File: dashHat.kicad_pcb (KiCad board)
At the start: 4 copper layers, 65 x 56 mm, 142 parts, among them J1 Input, J2 LCD, J3 GPIO, J4 LEDs, J5 Ride Through, J6 SMA, J7 Conn_01x08, Q1 BSS138, Q2 BSS138, Q3 2N7002, Q4 BSS84, Q5 BSS84, Q6 BSS84, Q7 , Q8 , U1 CAT24C256, U10 CPC1017N, U11 CPC1017N, U12 MAX22193, U13 IX4427, U2 MAX17614, U3 TVS3300DRV, U4 LM61480, U5 74LVC1G80, U6 ZOE-M8Q, U7 TCAN330, U8 MCP2515-xST, U9 MAX3227, Y1 32.768k, Y2 8MHz

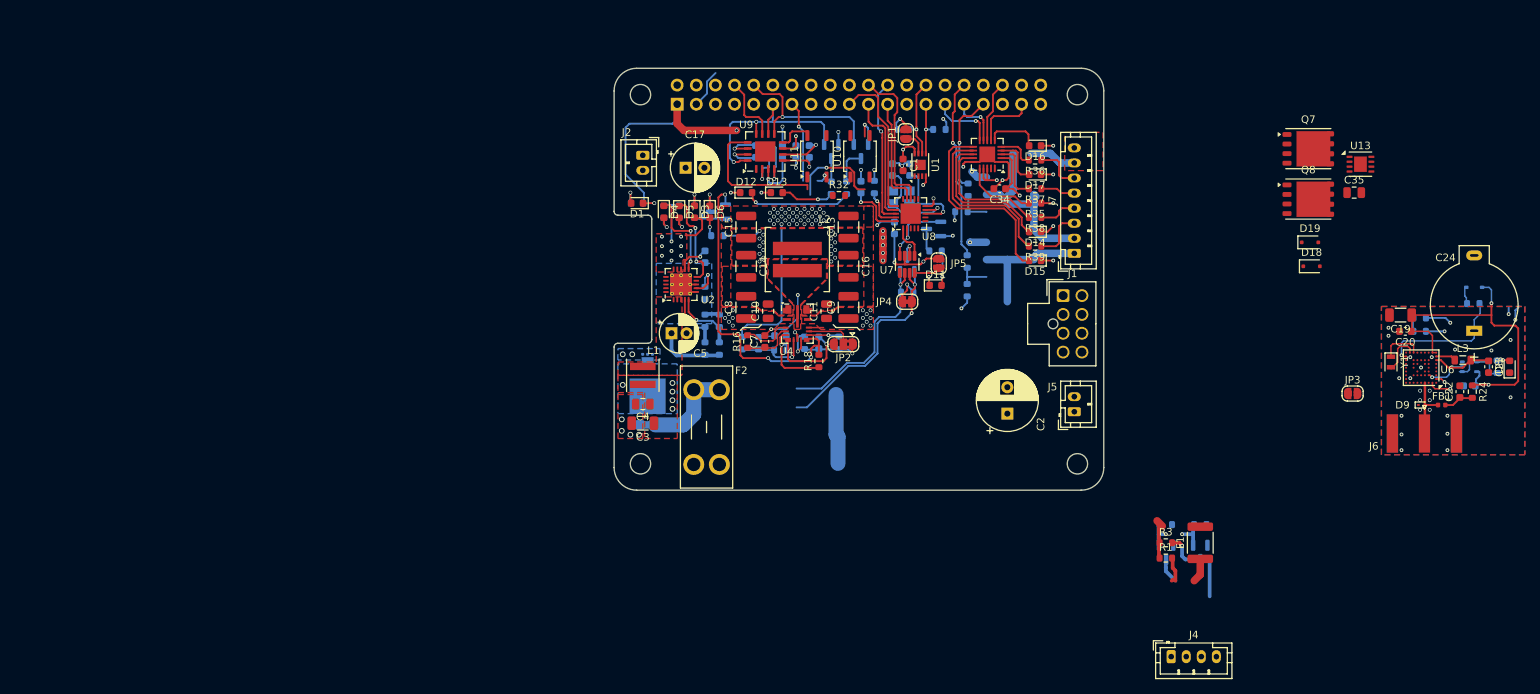
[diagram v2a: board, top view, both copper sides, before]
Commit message: second pass at layout complete
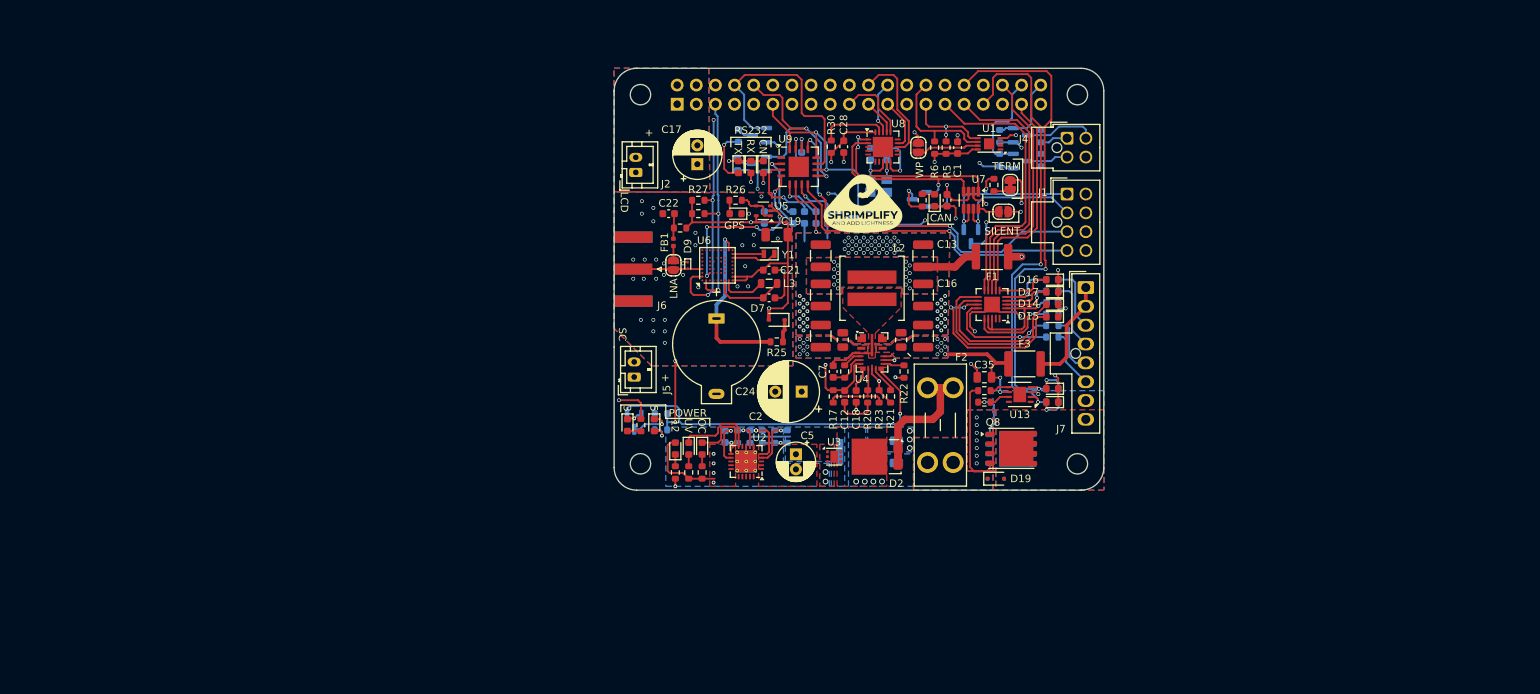
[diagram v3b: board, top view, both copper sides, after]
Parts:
- removed JP2: FPWM, Jumper:SolderJumper-3_P1.3mm_Bridged2Bar12_RoundedPad1.0x1.5mm
- removed R41, R43: 10k, Resistor_SMD:R_0603_1608Metric
- removed U10, U11: CPC1017N, Package_SO:SOP-4_3.8x4.1mm_P2.54mm
- added D20: Green, LED_SMD:LED_0603_1608Metric, F.Cu at (158.2, 86.5)
- added D21: Green, LED_SMD:LED_0603_1608Metric, F.Cu at (158.2, 88.3)
- added D22: Green, LED_SMD:LED_0603_1608Metric, F.Cu at (116.5, 57.1)
- added F3: 0.2A, Fuse:Fuse_1812_4532Metric, F.Cu at (154.5, 83.2)
- added Q9: BSS84, Package_TO_SOT_SMD:SOT-23, B.Cu at (119.3, 52.9)
- added R44: 1k, Resistor_SMD:R_0603_1608Metric, B.Cu at (158.2, 88.3)
- added R45: 1k, Resistor_SMD:R_0603_1608Metric, B.Cu at (158.2, 86.5)
- C12, C18, C21, C25, C28, D2, D7, R10, R11, R12, R17, R20, R21, R22, R23, R25, R26, R27, R28, R29, R30, R31, R40, R42, R5, R6, R7, U3, U5: moved to F.Cu
- C20, C3, C34, C4, D18, L1, Q7, R1, R18, R3, R35, R36, R37, R38, R39: moved to B.Cu
- J4: footprint Connector_JST:JST_PH_B4B-PH-K_1x04_P2.00mm_Vertical -> Connector_Molex:Molex_Nano-Fit_105310-xx04_2x02_P2.50mm_Vertical
- J7: footprint Connector_JST:JST_PH_B8B-PH-K_1x08_P2.00mm_Vertical -> Connector_Molex:Molex_Nano-Fit_105309-xx08_1x08_P2.50mm_Vertical
- R32: value 1k -> 220; moved to B.Cu
- moved C22 107.7 mm to (107.2, 63.3), turned to 180 degrees
- moved R24 107.4 mm to (108.8, 65.2), turned to 0 degrees
- moved J6 107.3 mm to (102.5, 70.7), turned to 180 degrees
- moved D8 104.7 mm to (116.1, 63.3), turned to 180 degrees
- moved FB1 104.2 mm to (107.9, 67.1), turned to 90 degrees
- moved R26 103.5 mm to (116.1, 61.5), turned to 180 degrees
- moved C24 100.6 mm to (113.6, 77.2), turned to -90 degrees
- moved D9 99.2 mm to (109.8, 70.2), turned to -90 degrees
- moved R27 97.0 mm to (111.2, 61.5)
- moved R28 97.0 mm to (111.2, 63.3)
- moved U5 96.0 mm to (119.8, 62.9), turned to 180 degrees
- moved C23 95.9 mm to (120.6, 74.5), turned to 0 degrees
- moved U6 94.4 mm to (113.7, 70.2), turned to 90 degrees
- moved C21 94.2 mm to (120.6, 70.8), turned to 0 degrees
- moved D7 92.7 mm to (121.6, 77.4), turned to 180 degrees
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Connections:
- D10 pad 1: /CAN/CANH -> /CAN/CANL
- D10 pad 2: /CAN/CANL -> /CAN/CANH
- D18 pad 1: /GPIO/+12V_{raw} -> +12P
- D19 pad 1: /GPIO/+12V_{raw} -> +12P
- F2 pad 1: /Power/+12V_{raw} -> +12P
- J1 pad 1: /RS232/232TX -> /CAN/CANL
- J1 pad 2: /RS232/232RX -> /CAN/CANH
- J1 pad 3: /CAN/CANH -> /RS232/232TX
- J1 pad 4: /CAN/CANL -> /RS232/232RX
- J1 pad 5: /GPIO/+12V_{raw} -> GND
- J1 pad 6: /GPIO/+12V_{raw} -> GND
- J1 pad 7: GND -> +12P
- J1 pad 8: GND -> +12P
- J7 pad 1: Net-(D19-A) -> Net-(J7-Pin_1)
- J7 pad 2: Net-(D18-A) -> Net-(J7-Pin_1)
- J7 pad 7: +12V -> Net-(D18-A)
- J7 pad 8: +12V -> Net-(D19-A)
- Q7 pad 1: Net-(Q7-G) -> GND
- Q7 pad 2: Net-(D18-A) -> Net-(Q7-G)
- Q7 pad 3: GND -> Net-(D18-A)
- Q8 pad 1: Net-(Q8-G) -> GND
- Q8 pad 2: Net-(D19-A) -> Net-(Q8-G)
- Q8 pad 3: GND -> Net-(D19-A)
- R1 pad 1: +5V -> Net-(J4-Pin_1)
- R3 pad 1: +5V -> Net-(J4-Pin_1)
- R32 pad 1: /GPIO27 -> Net-(Q9-D)
- R36 pad 1: Net-(J7-Pin_6) -> Net-(J7-Pin_3)
- R37 pad 1: Net-(J7-Pin_5) -> Net-(J7-Pin_4)
- R38 pad 1: Net-(J7-Pin_4) -> Net-(J7-Pin_5)
- R38 pad 2: Net-(U12-IN4) -> Net-(U12-IN3)
- R39 pad 1: Net-(J7-Pin_3) -> Net-(J7-Pin_6)
- R39 pad 2: Net-(U12-IN3) -> Net-(U12-IN4)
- U12 pad 11: Net-(D15-A) -> Net-(D14-A)
- U12 pad 13: Net-(D14-A) -> Net-(D15-A)
- U4 pad 12: Net-(JP2-C) -> GND
- U9 pad 13: Net-(U9-T1OUT) -> /RS232/232TX
- U9 pad 8: Net-(U9-R1IN) -> /RS232/232RX
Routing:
- net /RS232/232TX: track 0.00 -> 49.2 mm, vias 0 -> 3
- net /GPIO13/PWM1: track 13.3 -> 61.1 mm, vias 1 -> 2
- net /RS232/232RX: track 0.00 -> 41.8 mm, vias 0 -> 1
- net +12V: track 68.6 -> 28.0 mm, vias 23 -> 22
- net /GPIO12/PWM0: track 23.9 -> 62.9 mm, vias 1 -> 2
- net +3V3: track 144.3 -> 183.0 mm, vias 18 -> 15
- net (no net): track 30.2 -> 0.00 mm, vias 1 -> 0
- net /GPIO5: track 8.70 -> 37.3 mm, vias 1 -> 0
- net /GPIO6: track 7.04 -> 35.6 mm, vias 1 -> 0
- net /GPIO16: track 8.17 -> 33.2 mm
- net Net-(J4-Pin_1): track 3.14 -> 28.0 mm, vias 0 -> 1
- net Net-(D18-A): track 24.4 -> 0.00 mm
- net /GPIO14/TXD0: track 8.98 -> 33.0 mm
- net Net-(U7-TXD): track 4.71 -> 26.3 mm, vias 0 -> 2
- net /GPIO26: track 8.41 -> 29.9 mm
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- added copper zone on B.Cu, net +12P
- added copper zone on F.Cu, net +12P
- added copper zone on In2.Cu, net +12P
- added copper zone on B.Cu, net +12V
- added copper zone on In1.Cu, net +12V
- added copper zone on B.Cu, net +5V
- added copper zone on In1.Cu, net +5V
- added copper zone on In2.Cu, net GND
- added copper zone on B.Cu, net IN
- added copper zone on B.Cu, net Net-(D18-A)
- added copper zone on F.Cu, net Net-(D19-A)
- removed copper zone on F.Cu, net /GPIO/+12V_{raw}
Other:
- outline, holes or cut-outs redrawn
- board text added: "+"
- board text added: "12"
- board text added: "3"
- board text added: "5"
- board text added: "CAN"
- board text added: "CN"
- board text added: "GPS"
- board text added: "LCD"
- board text added: "LNA"
- board text added: "OC"
- board text added: "POWER"
- board text added: "RS232"
- board text added: "RX"
- board text added: "SC"
- board text added: "SILENT"
- board text added: "TERM"
- board text added: "TX"
- board text added: "UV"
- board text added: "WP"
- board text removed: "DISPLAY (OPTIONAL)"
- board text removed: "Extend PCB edge 0.5mm if using SMT header"
- board text removed: "RJ45"
- board text removed: "USB"

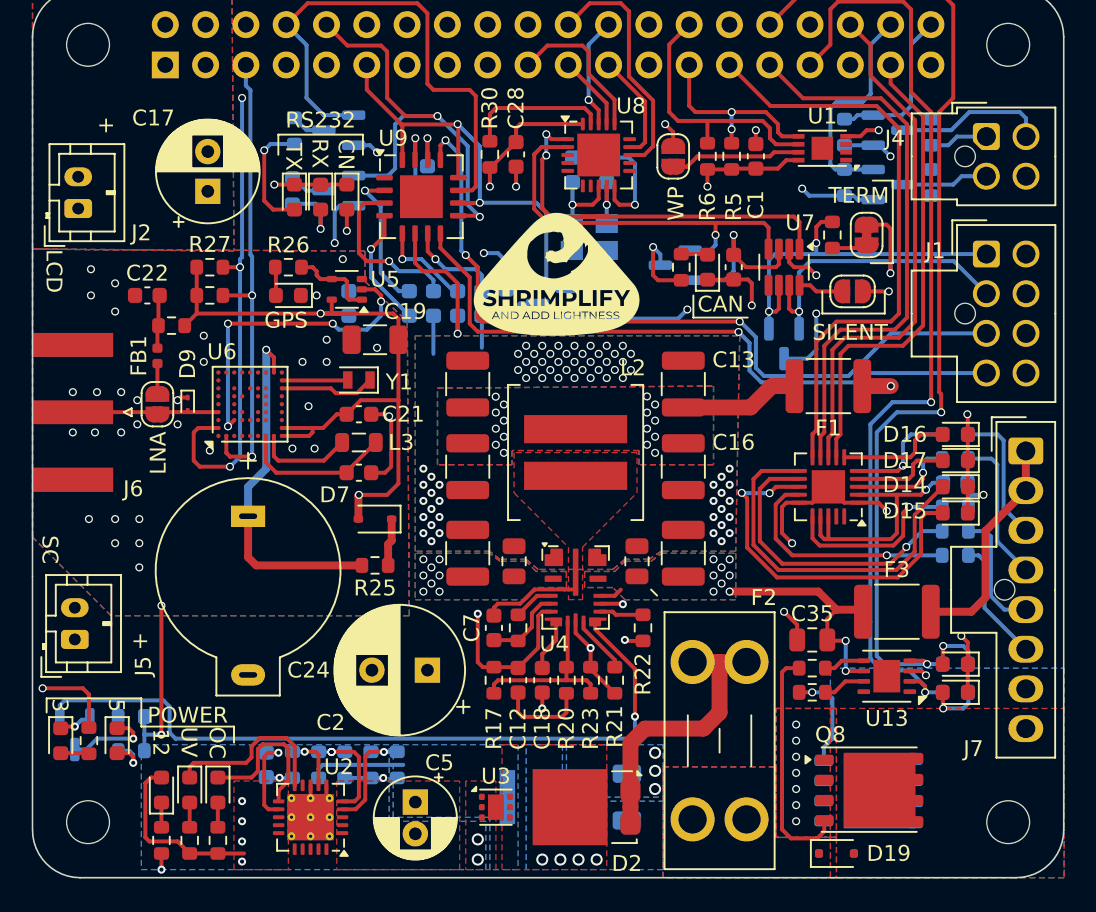
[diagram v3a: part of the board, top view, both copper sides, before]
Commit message: add a version, add uart test pads to gps, sent for manufacturing
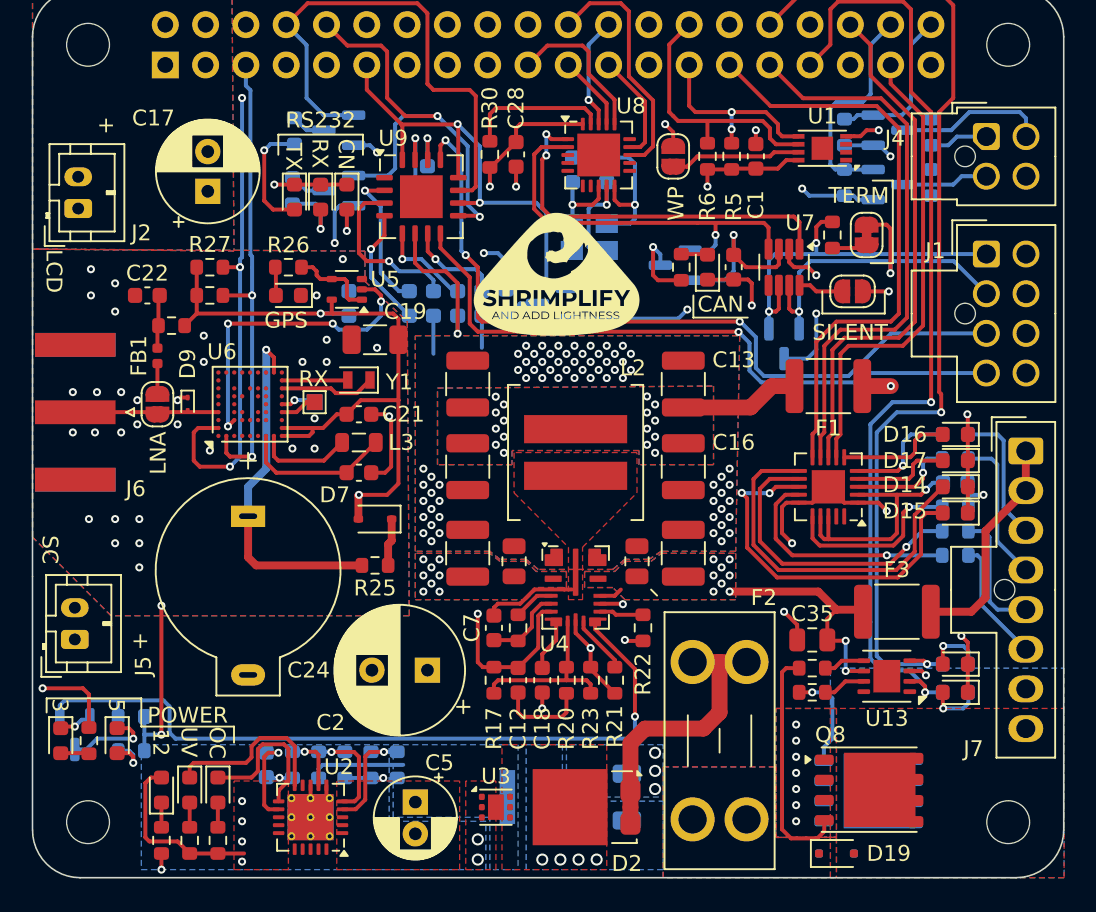
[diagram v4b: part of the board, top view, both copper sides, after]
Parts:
- added TP1: TestPoint, TestPoint:TestPoint_Pad_1.0x1.0mm, B.Cu at (117.8, 70.0)
- added TP2: TestPoint, TestPoint:TestPoint_Pad_1.0x1.0mm, F.Cu at (117.8, 70.0)
- Q1, Q2: value BSS138 -> 2N7002
- moved J6 0.16 mm to (102.7, 70.7)
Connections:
- U6 pad J4: unconnected-(U6-RXD/SPI_MOSI-PadJ4) -> Net-(U6-RXD/SPI_MOSI)
- U6 pad J5: unconnected-(U6-TXD/SPI_MISO-PadJ5) -> Net-(U6-TXD/SPI_MISO)
- Y2 pad 2: Net-(U8-OSC1) -> GND
- Y2 pad 3: (no net) -> Net-(U8-OSC1)
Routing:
- net Net-(U8-OSC1): track 3.79 -> 7.50 mm
- net GND: track 89.7 -> 92.5 mm
- net Net-(U6-RXD/SPI_MOSI): track 0.00 -> 2.32 mm
- net Net-(U6-TXD/SPI_MISO): track 0.00 -> 2.22 mm, vias 0 -> 1
- net Net-(U2-OVLO): vias 2 -> 1
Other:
- board text added: "MLB - REV 1 05/2024"

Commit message: added missing 3d models, fussed with the silkscreen more
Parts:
- moved FB1 3.05 mm to (107.9, 70.2)
- moved JP3 2.67 mm to (107.9, 67.5), turned to -90 degrees
- moved J6 0.38 mm to (103.1, 70.7)
- moved R24 0.25 mm to (108.8, 64.9)
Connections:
- C22 pad 1: Net-(C22-Pad1) -> Net-(JP3-A)
- FB1 pad 1: Net-(JP3-B) -> Net-(D9-A2)
- FB1 pad 2: Net-(C22-Pad1) -> Net-(JP3-B)
- JP3 pad 1: Net-(D9-A2) -> Net-(JP3-A)
- R24 pad 1: Net-(C22-Pad1) -> Net-(JP3-A)
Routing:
- net Net-(JP3-A): track 0.00 -> 3.68 mm
- net Net-(C22-Pad1): track 3.12 -> 0.00 mm
- net +3V3: track 183.0 -> 182.3 mm
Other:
- board text added: "INPUTS"
- board text added: "OUTPUTS"

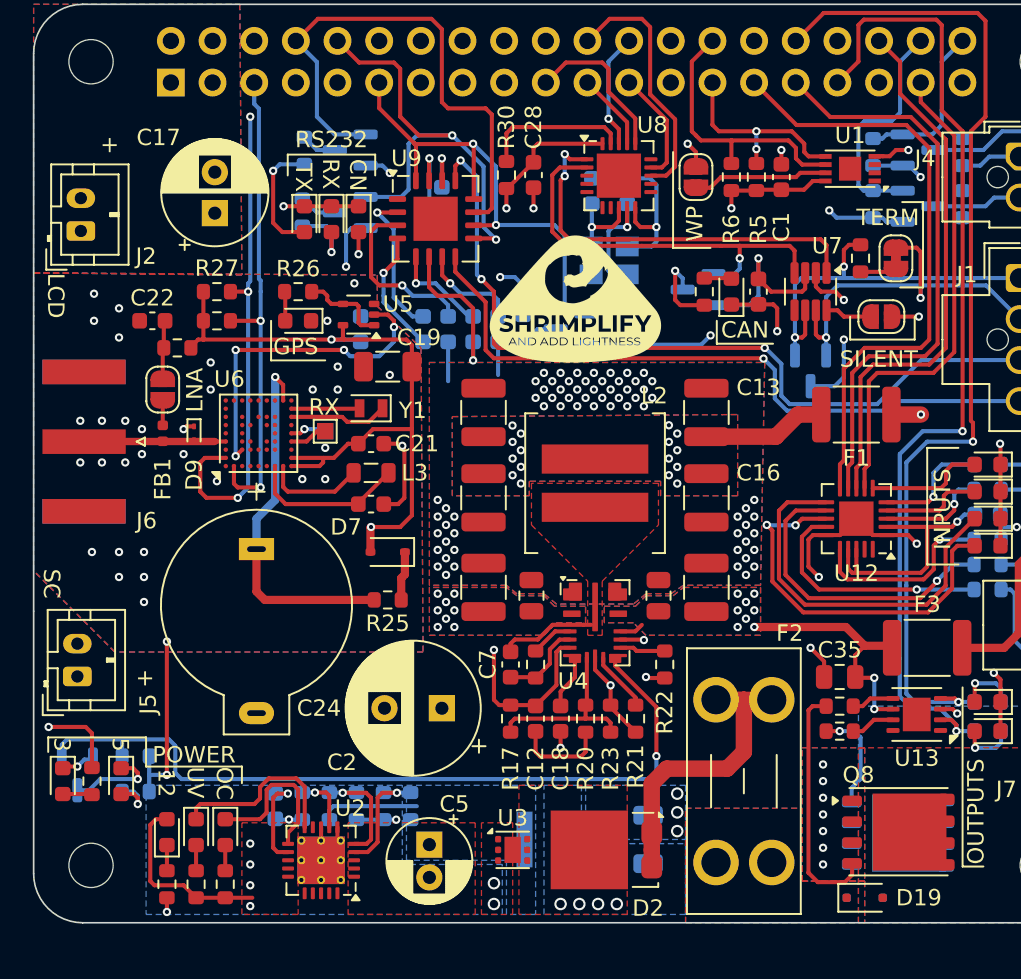
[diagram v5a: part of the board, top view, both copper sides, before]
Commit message: bug fixes from testing
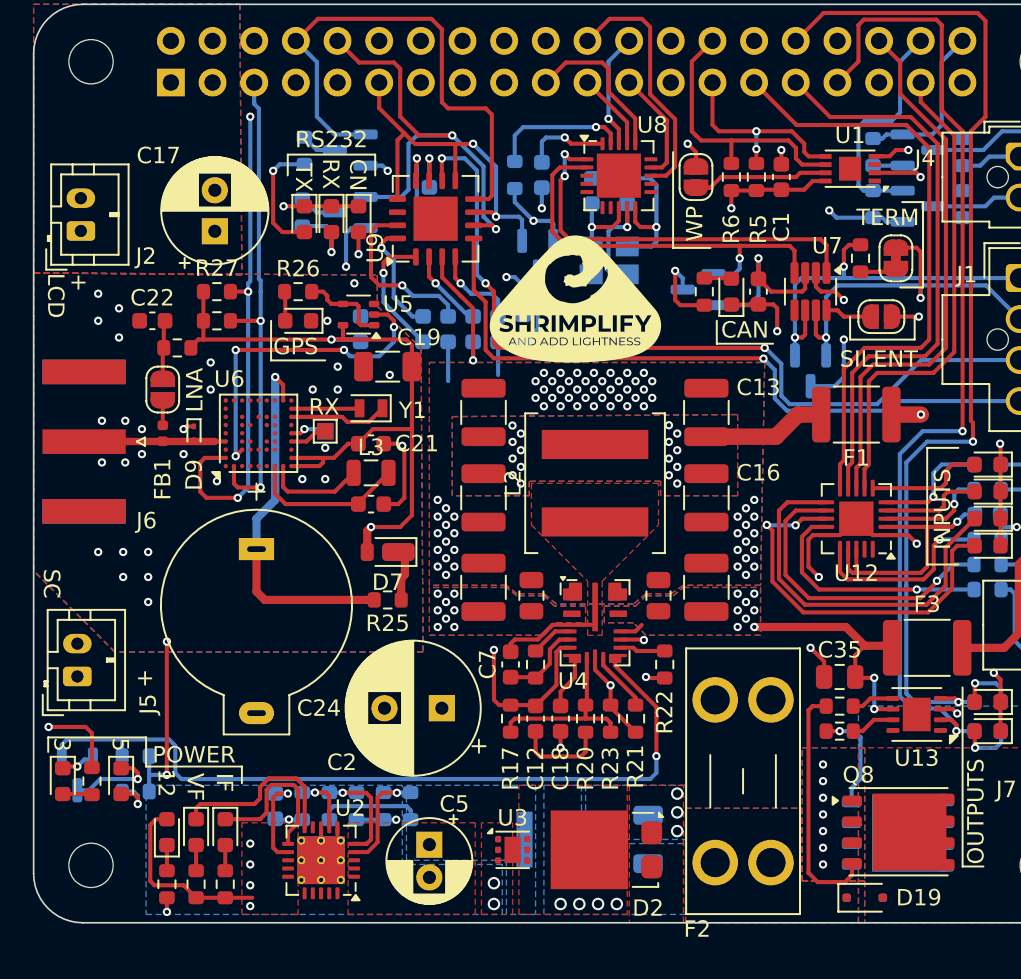
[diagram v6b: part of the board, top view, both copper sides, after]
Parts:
- C28, R30: moved to B.Cu
- D7: footprint Diode_SMD:D_SOD-323 -> Custom:D_SOD-323HE
- L2: footprint Inductor_SMD:L_Coilcraft_XAL7030-272 -> Custom:L_Coilcraft_XAL7030-272
- L3: footprint Inductor_SMD:L_0805_2012Metric -> Custom:L_0806_2016Metric
- Q1, Q2: value 2N7002 -> BSS138
- moved F2 10.5 mm to (145.0, 86.4), turned to -90 degrees
- moved Q6 4.89 mm to (130.7, 59.4), turned to -90 degrees
- moved R13 3.30 mm to (123.0, 92.9)
- moved R14 3.30 mm to (118.0, 92.9)
- moved R8 3.30 mm to (121.3, 92.9)
- moved R9 3.30 mm to (119.7, 92.9)
- moved C17 1.10 mm to (111.0, 57.8)
- moved C33 0.76 mm to (124.1, 55.9)
- moved C28 0.51 mm to (131.0, 54.4)
- moved R30 0.51 mm to (129.3, 54.4)
- turned U9 to 90 degrees
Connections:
- C3 pad 1: Net-(D2-K) -> +12P
- C4 pad 1: Net-(D2-K) -> +12P
- D2 pad 1: Net-(D2-K) -> +12P
- D2 pad 2: Net-(D2-A) -> GND
- F2 pad 1: +12P -> /Power/+12v_raw
- F2 pad 2: Net-(D2-A) -> +12P
- J1 pad 7: +12P -> /Power/+12v_raw
- J1 pad 8: +12P -> /Power/+12v_raw
- L1 pad 1: Net-(D2-K) -> +12P
- R13 pad 1: Net-(U2-OVLO) -> Net-(U2-UVLO)
- R14 pad 1: Net-(U2-UVLO) -> Net-(U2-OVLO)
- R8 pad 2: Net-(U2-OVLO) -> Net-(U2-UVLO)
- R9 pad 2: Net-(U2-UVLO) -> Net-(U2-OVLO)
- U1 pad 2: unconnected-(U1-A1-Pad2) -> +3V3
- U3 pad 4: Net-(D2-K) -> +12P
- U3 pad 5: Net-(D2-K) -> +12P
- U3 pad 6: Net-(D2-K) -> +12P
- U9 pad 1: unconnected-(U9-READY-Pad1) -> Net-(U9-C1-)
- U9 pad 10: /GPIO17 -> /RS232/232TX
- U9 pad 11: /GPIO14/TXD0 -> GND
- U9 pad 12: /GPIO17 -> +3V3
- U9 pad 13: /RS232/232TX -> /GPIO17
- U9 pad 14: GND -> unconnected-(U9-READY-Pad14)
- U9 pad 15: +3V3 -> Net-(U9-V+)
- U9 pad 16: /GPIO17 -> Net-(U9-C1+)
- U9 pad 2: Net-(U9-C1+) -> Net-(U9-C2+)
- U9 pad 3: Net-(U9-V+) -> Net-(U9-C2-)
- U9 pad 4: Net-(U9-C1-) -> Net-(U9-V-)
- U9 pad 5: Net-(U9-C2+) -> /RS232/232RX
- U9 pad 6: Net-(U9-C2-) -> /GPIO15/RXD0
- U9 pad 7: Net-(U9-V-) -> /GPIO17
- U9 pad 8: /RS232/232RX -> /GPIO14/TXD0
- U9 pad 9: /GPIO15/RXD0 -> /GPIO17
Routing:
- net Net-(D2-A): track 18.1 -> 0.00 mm
- net /GPIO17: track 31.2 -> 24.1 mm
- net +5V: track 96.3 -> 90.7 mm
- net GND: track 92.3 -> 96.1 mm, vias 134 -> 131
- net +3V3: track 182.3 -> 178.6 mm
- net IN: track 6.01 -> 2.42 mm, vias 0 -> 1
- net Net-(Q6-D): track 2.08 -> 4.74 mm
- net Net-(U9-C1+): track 9.11 -> 6.97 mm
- net /RS232/232TX: track 49.2 -> 50.6 mm
- net Net-(U9-C2-): track 9.37 -> 8.22 mm
- net Net-(U9-C2+): track 5.93 -> 4.90 mm
- net /GPIO14/TXD0: track 33.0 -> 32.2 mm
- net Net-(U9-V-): track 6.16 -> 5.46 mm
- net /RS232/232RX: track 41.8 -> 42.5 mm
- net /GPIO15/RXD0: track 28.4 -> 27.9 mm
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- added copper zone on In2.Cu, net /Power/+12v_raw
- removed copper zone on In2.Cu, net +12P
- removed copper zone on B.Cu, net Net-(D2-K)
- removed copper zone on F.Cu, net Net-(D2-K)
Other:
- board text added: "IF"
- board text added: "MLB - REV 2 05/2024"
- board text added: "VF"
- board text removed: "MLB - REV 1 05/2024"
- board text removed: "OC"
- board text removed: "UV"
